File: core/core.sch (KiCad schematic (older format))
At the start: 1 part

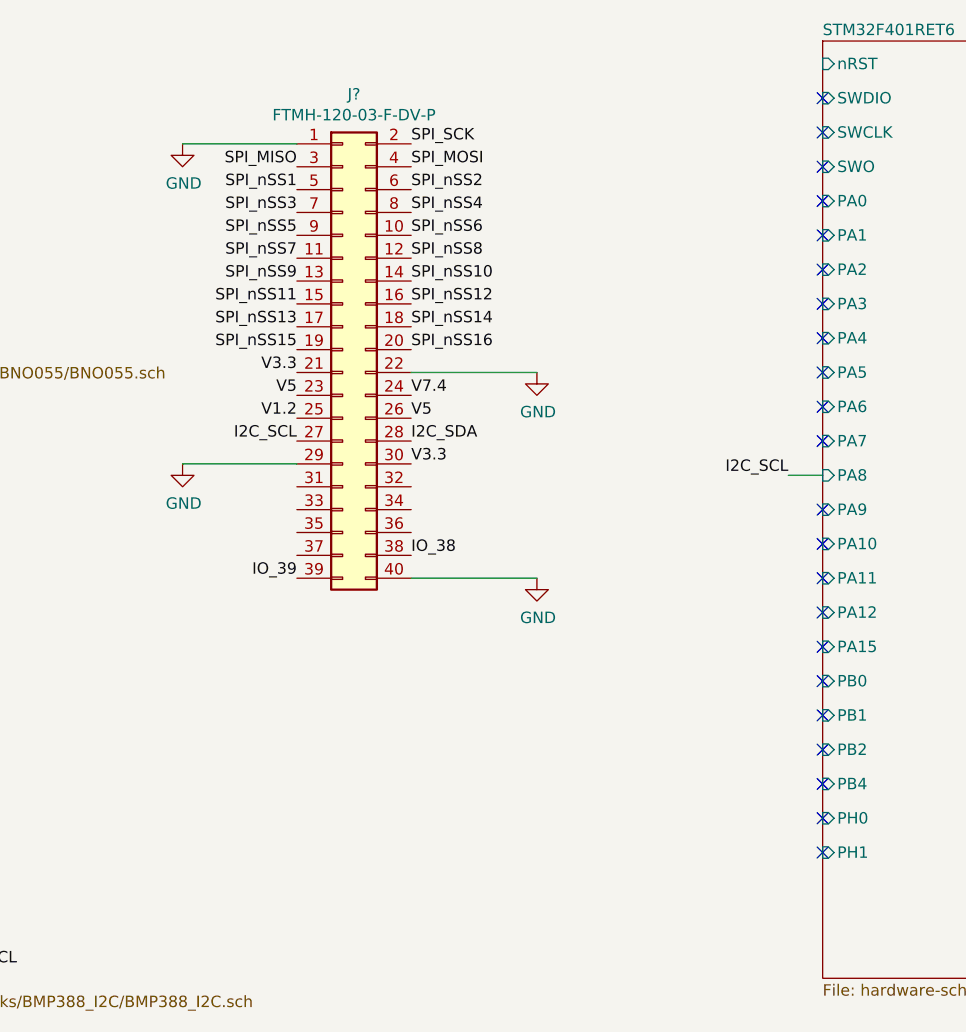
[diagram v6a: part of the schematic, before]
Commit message: Add CAS bus sheet to core
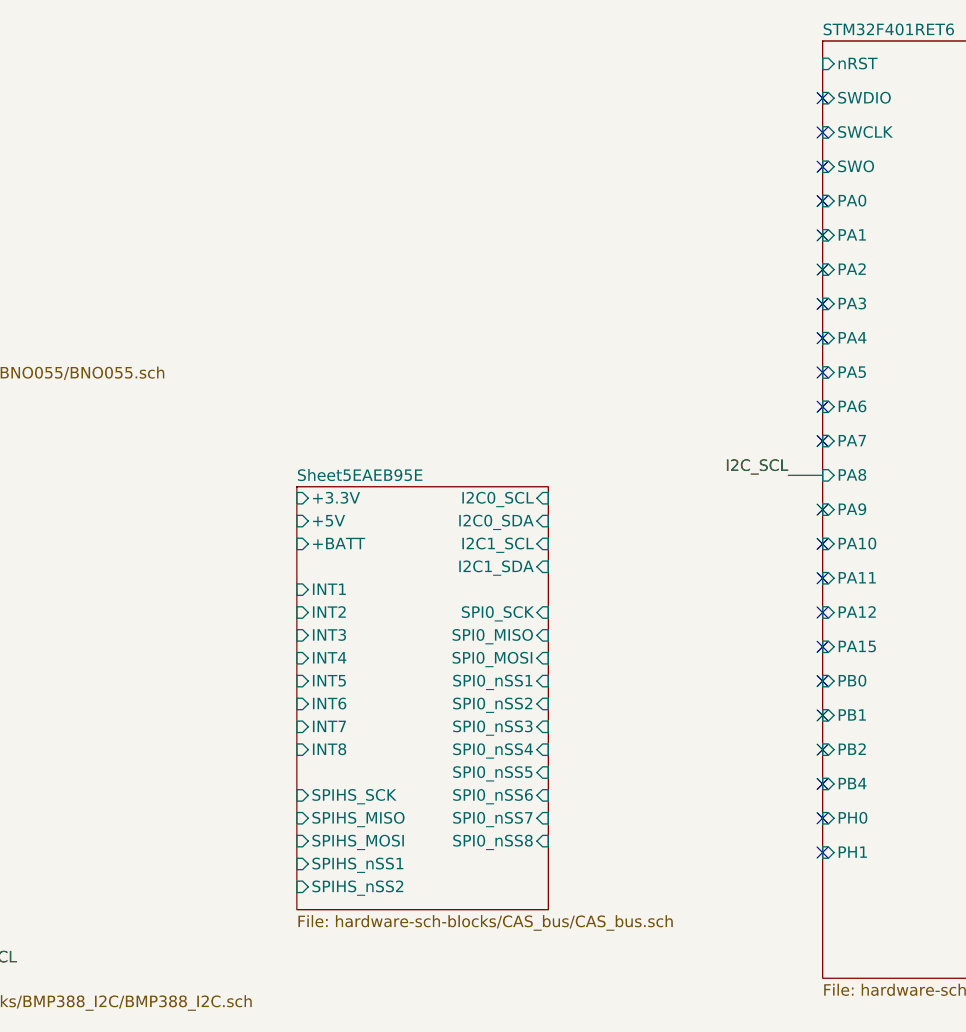
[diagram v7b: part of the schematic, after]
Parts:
- removed J?: FTMH-120-03-F-DV-P, symbol core-rescue:FTMH-120-03-F-DV-P-star-common-lib
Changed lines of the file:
@@
 $Descr A4 11693 8268
 encoding utf-8
-Sheet 1 4
+Sheet 1 5
 Title ""
 Date ""
@@
 Wire Wire Line
 	3700 5550 3600 5550
-$Comp
-L core-rescue:FTMH-120-03-F-DV-P-star-common-lib J?
-U 1 1 5E646F14
-P 5400 2850
-F 0 "J?" H 5450 3967 50  0000 C CNN
-F 1 "FTMH-120-03-F-DV-P" H 5450 3876 50  0000 C CNN
-F 2 "" H 5400 2850 50  0001 C CNN
-F 3 "~" H 5400 2850 50  0001 C CNN
-	1    5400 2850
-	1    0    0    -1
-$EndComp
 Text Label 7350 3400 2    50   ~ 0
 I2C_SCL
@@
 Text Label 8550 4600 0    50   ~ 0
 I2C_SDA
-Text Label 5700 3750 0    50   ~ 0
-IO_38
-Text Label 5200 2050 2    50   ~ 0
-SPI_MISO
-Text Label 5200 2150 2    50   ~ 0
-SPI_nSS1
-Text Label 5200 2250 2    50   ~ 0
-SPI_nSS3
-Text Label 5200 2350 2    50   ~ 0
-SPI_nSS5
-Text Label 5200 2450 2    50   ~ 0
-SPI_nSS7
-Text Label 5200 2550 2    50   ~ 0
-SPI_nSS9
-Text Label 5200 2650 2    50   ~ 0
-SPI_nSS11
-Text Label 5200 2750 2    50   ~ 0
-SPI_nSS13
-Text Label 5200 2850 2    50   ~ 0
-SPI_nSS15
-Text Label 5700 1950 0    50   ~ 0
-SPI_SCK
-Text Label 5700 2050 0    50   ~ 0
-SPI_MOSI
-Text Label 5700 2150 0    50   ~ 0
-SPI_nSS2
-Text Label 5700 2250 0    50   ~ 0
-SPI_nSS4
-Text Label 5700 2350 0    50   ~ 0
-SPI_nSS6
-Text Label 5700 2450 0    50   ~ 0
-SPI_nSS8
-Text Label 5700 2550 0    50   ~ 0
-SPI_nSS10
-Text Label 5700 2650 0    50   ~ 0
-SPI_nSS12
-Text Label 5700 2750 0    50   ~ 0
-SPI_nSS14
-Text Label 5200 2950 2    50   ~ 0
-V3.3
-Text Label 5200 3050 2    50   ~ 0
-V5
-Text Label 5700 2850 0    50   ~ 0
-SPI_nSS16
-Text Label 5700 3050 0    50   ~ 0
-V7.4
-$Comp
-L power:GND #PWR?
-U 1 1 5E652AC2
-P 6250 2950
-F 0 "#PWR?" H 6250 2700 50  0001 C CNN
-F 1 "GND" H 6255 2777 50  0000 C CNN
-F 2 "" H 6250 2950 50  0001 C CNN
-F 3 "" H 6250 2950 50  0001 C CNN
-	1    6250 2950
-	1    0    0    -1
-$EndComp
-Wire Wire Line
-	5700 2950 6250 2950
-Text Label 5200 3850 2    50   ~ 0
-IO_39
-Text Label 5200 3250 2    50   ~ 0
-I2C_SCL
-Text Label 5700 3250 0    50   ~ 0
-I2C_SDA
-$Comp
-L power:GND #PWR?
-U 1 1 5E65479A
-P 4700 1950
-F 0 "#PWR?" H 4700 1700 50  0001 C CNN
-F 1 "GND" H 4705 1777 50  0000 C CNN
-F 2 "" H 4700 1950 50  0001 C CNN
-F 3 "" H 4700 1950 50  0001 C CNN
-	1    4700 1950
-	1    0    0    -1
-$EndComp
-Wire Wire Line
-	4700 1950 5200 1950
-Text Label 5200 3150 2    50   ~ 0
-V1.2
-$Comp
-L power:GND #PWR?
-U 1 1 5E656A75
-P 6250 3850
-F 0 "#PWR?" H 6250 3600 50  0001 C CNN
-F 1 "GND" H 6255 3677 50  0000 C CNN
-F 2 "" H 6250 3850 50  0001 C CNN
-F 3 "" H 6250 3850 50  0001 C CNN
-	1    6250 3850
-	1    0    0    -1
-$EndComp
-Wire Wire Line
-	6250 3850 5700 3850
-Wire Wire Line
-	4700 3350 5200 3350
-$Comp
-L power:GND #PWR?
-U 1 1 5E657C0D
-P 4700 3350
-F 0 "#PWR?" H 4700 3100 50  0001 C CNN
-F 1 "GND" H 4705 3177 50  0000 C CNN
-F 2 "" H 4700 3350 50  0001 C CNN
-F 3 "" H 4700 3350 50  0001 C CNN
-	1    4700 3350
-	1    0    0    -1
-$EndComp
-Text Label 5700 3350 0    50   ~ 0
-V3.3
-Text Label 5700 3150 0    50   ~ 0
-V5
 $Sheet
 S 7500 1500 900  4100
@@
 F5 "SCL" O R 3600 5550 50
 $EndSheet
+$Sheet
+S 5200 3450 1100 1850
+U 5EAEB95F
+F0 "Sheet5EAEB95E" 50
+F1 "hardware-sch-blocks/CAS_bus/CAS_bus.sch" 50
+F2 "INT1" I L 5200 3900 50
+F3 "INT3" I L 5200 4100 50
+F4 "INT5" I L 5200 4300 50
+F5 "I2C0_SCL" I R 6300 3500 50
+F6 "I2C1_SCL" I R 6300 3700 50
+F7 "INT7" I L 5200 4500 50
+F8 "SPI0_nSS1" I R 6300 4300 50
+F9 "SPI0_SCK" I R 6300 4000 50
+F10 "SPI0_MISO" I R 6300 4100 50
+F11 "SPI0_MOSI" I R 6300 4200 50
+F12 "INT2" I L 5200 4000 50
+F13 "INT4" I L 5200 4200 50
+F14 "INT6" I L 5200 4400 50
+F15 "I2C0_SDA" I R 6300 3600 50
+F16 "I2C1_SDA" I R 6300 3800 50
+F17 "INT8" I L 5200 4600 50
+F18 "SPI0_nSS2" I R 6300 4400 50
+F19 "SPI0_nSS3" I R 6300 4500 50
+F20 "SPI0_nSS4" I R 6300 4600 50
+F21 "SPI0_nSS5" I R 6300 4700 50
+F22 "SPI0_nSS6" I R 6300 4800 50
+F23 "SPI0_nSS7" I R 6300 4900 50
+F24 "SPI0_nSS8" I R 6300 5000 50
+F25 "SPIHS_SCK" I L 5200 4800 50
+F26 "SPIHS_MISO" I L 5200 4900 50
+F27 "SPIHS_MOSI" I L 5200 5000 50
+F28 "SPIHS_nSS1" I L 5200 5100 50
+F29 "SPIHS_nSS2" I L 5200 5200 50
+F30 "+3.3V" I L 5200 3500 50
+F31 "+5V" I L 5200 3600 50
+F32 "+BATT" I L 5200 3700 50
+$EndSheet
 $EndSCHEMATC

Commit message: SPI/I2C boilerplate
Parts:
- added R1, R2, R3, R4: 10k, symbol Device:R_US
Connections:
- new net +3V3: R1.1, R2.1, R3.1, R4.1
- new net I2C0_SCL: R1.2
- new net I2C0_SDA: R2.2
- new net I2C1_SCL: R4.2
- new net I2C1_SDA: R3.2
- no-connect marks 44 -> 36
